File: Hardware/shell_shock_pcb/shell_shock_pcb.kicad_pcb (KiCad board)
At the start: 2 copper layers, 30 parts, among them U14 LT3080EDD-PBF, U23 LT3080EDD-PBF, U4 LT3080EDD-PBF, U5 LT3080EDD-PBF

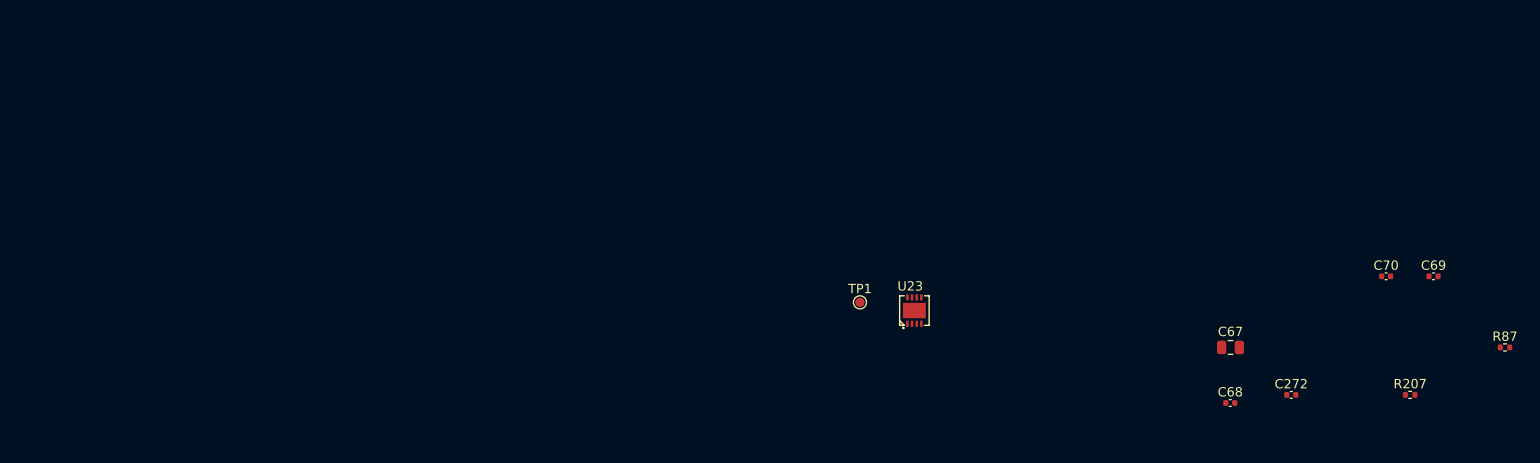
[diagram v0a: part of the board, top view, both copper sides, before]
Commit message: Added hardware tools
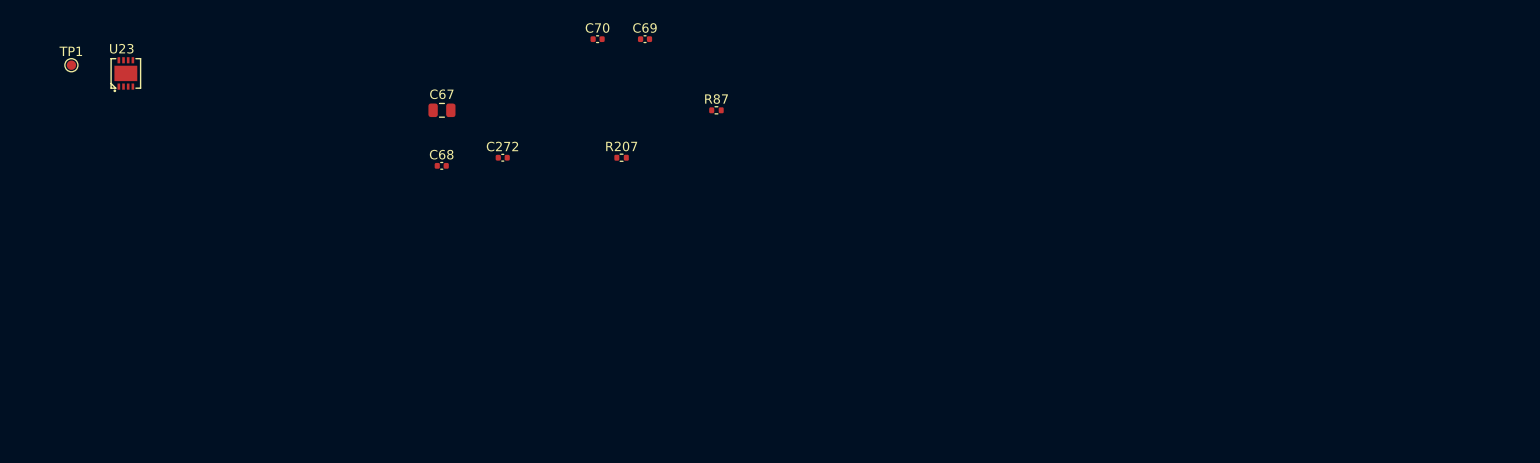
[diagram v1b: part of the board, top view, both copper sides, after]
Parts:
- moved C68 88.2 mm to (145.7, 82.1)
- moved C69 88.2 mm to (167.5, 68.6)
- moved C70 88.2 mm to (162.4, 68.6)
- moved R207 88.2 mm to (165.0, 81.3)
- moved U23 88.2 mm to (111.9, 72.2)
- moved C67 88.2 mm to (145.7, 76.2)
- moved C272 88.2 mm to (152.2, 81.3)
- moved TP1 88.2 mm to (106.0, 71.4)
- moved R87 88.2 mm to (175.1, 76.2)
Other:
- board text added: "1.5V - PS"
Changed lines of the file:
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@@
   (net 13 "unconnected-(U23-NC-Pad6)")
   (footprint "Capacitor_SMD:C_0402_1005Metric" (layer "F.Cu")
-    (at 236.7 106.68)
+    (at 152.24 81.28)
     (descr "Capacitor SMD 0402 (1005 Metric), square (rectangular) end terminal, IPC_7351 nominal, (Body size source: IPC-SM-782 page 76, https://www.pcb-3d.com/wordpress/wp-content/uploads/ipc-sm-782a_amendment_1_and_2.pdf), generated with kicad-footprint-generator")
     (tags "capacitor")
@@
   )
   (footprint "Capacitor_SMD:C_0402_1005Metric" (layer "F.Cu")
-    (at 251.94 93.98)
+    (at 167.48 68.58)
     (descr "Capacitor SMD 0402 (1005 Metric), square (rectangular) end terminal, IPC_7351 nominal, (Body size source: IPC-SM-782 page 76, https://www.pcb-3d.com/wordpress/wp-content/uploads/ipc-sm-782a_amendment_1_and_2.pdf), generated with kicad-footprint-generator")
     (tags "capacitor")
@@
   )
   (footprint "Capacitor_SMD:C_0402_1005Metric" (layer "F.Cu")
-    (at 230.166096 107.549422)
+    (at 145.706096 82.149422)
     (descr "Capacitor SMD 0402 (1005 Metric), square (rectangular) end terminal, IPC_7351 nominal, (Body size source: IPC-SM-782 page 76, https://www.pcb-3d.com/wordpress/wp-content/uploads/ipc-sm-782a_amendment_1_and_2.pdf), generated with kicad-footprint-generator")
     (tags "capacitor")
@@
   )
   (footprint "Capacitor_SMD:C_0402_1005Metric" (layer "F.Cu")
-    (at 246.86 93.98)
+    (at 162.4 68.58)
     (descr "Capacitor SMD 0402 (1005 Metric), square (rectangular) end terminal, IPC_7351 nominal, (Body size source: IPC-SM-782 page 76, https://www.pcb-3d.com/wordpress/wp-content/uploads/ipc-sm-782a_amendment_1_and_2.pdf), generated with kicad-footprint-generator")
     (tags "capacitor")
@@
   )
   (footprint "Resistor_SMD:R_0402_1005Metric" (layer "F.Cu")
-    (at 249.43 106.68)
+    (at 164.97 81.28)
     (descr "Resistor SMD 0402 (1005 Metric), square (rectangular) end terminal, IPC_7351 nominal, (Body size source: IPC-SM-782 page 72, https://www.pcb-3d.com/wordpress/wp-content/uploads/ipc-sm-782a_amendment_1_and_2.pdf), generated with kicad-footprint-generator")
     (tags "resistor")
@@
   )
   (footprint "Resistor_SMD:R_0402_1005Metric" (layer "F.Cu")
-    (at 259.59 101.6)
+    (at 175.13 76.2)
     (descr "Resistor SMD 0402 (1005 Metric), square (rectangular) end terminal, IPC_7351 nominal, (Body size source: IPC-SM-782 page 72, https://www.pcb-3d.com/wordpress/wp-content/uploads/ipc-sm-782a_amendment_1_and_2.pdf), generated with kicad-footprint-generator")
     (tags "resistor")
@@
   )
   (footprint "TestPoint:TestPoint_Pad_D1.0mm" (layer "F.Cu")
-    (at 190.5 96.77)
+    (at 106.04 71.37)
     (descr "SMD pad as test Point, diameter 1.0mm")
     (tags "test point SMD pad")
@@
   )
   (footprint "Capacitor_SMD:C_0805_2012Metric" (layer "F.Cu")
-    (at 230.19 101.6)
+    (at 145.73 76.2)
     (descr "Capacitor SMD 0805 (2012 Metric), square (rectangular) end terminal, IPC_7351 nominal, (Body size source: IPC-SM-782 page 76, https://www.pcb-3d.com/wordpress/wp-content/uploads/ipc-sm-782a_amendment_1_and_2.pdf, https://docs.google.com/spreadsheets/d/1BsfQQcO9C6DZCsRaXUlFlo91Tg2WpOkGARC1WS5S8t0/edit?usp=sharing), generated with kicad-footprint-generator")
     (tags "capacitor")
@@
   )
   (footprint "LCSC:DFN-8_L3.0-W3.0-P0.50-BL-EP" (layer "F.Cu")
-    (at 196.33 97.65)
+    (at 111.87 72.25)
     (property "LCSC" "C462675")
     (property "Sheetfile" "shell_shock_pcb.kicad_sch")
@@
     (effects (font (size 1 1) (thickness 0.15)) (justify left bottom))
   )
-  (gr_text "1.8V - PS" (at 43.425782 194.156525) (layer "Dwgs.User")
+  (gr_text "1.5V - PS" (at 43.425782 194.156525) (layer "Dwgs.User")
     (effects (font (size 1 1) (thickness 0.15)) (justify left bottom))
   )

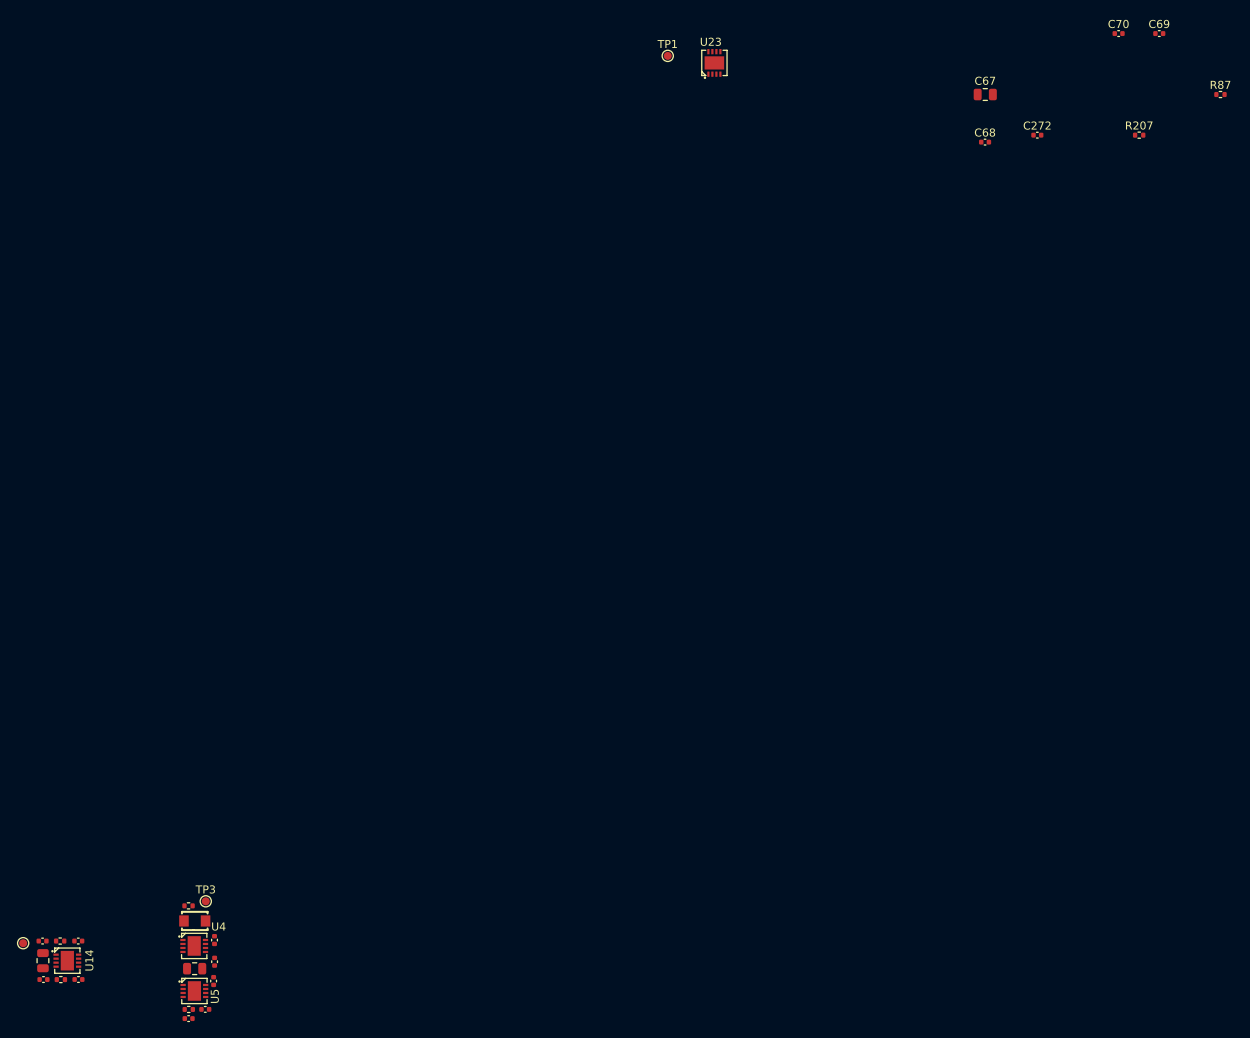
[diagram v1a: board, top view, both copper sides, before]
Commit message: sketch pcb for LT3080 ps
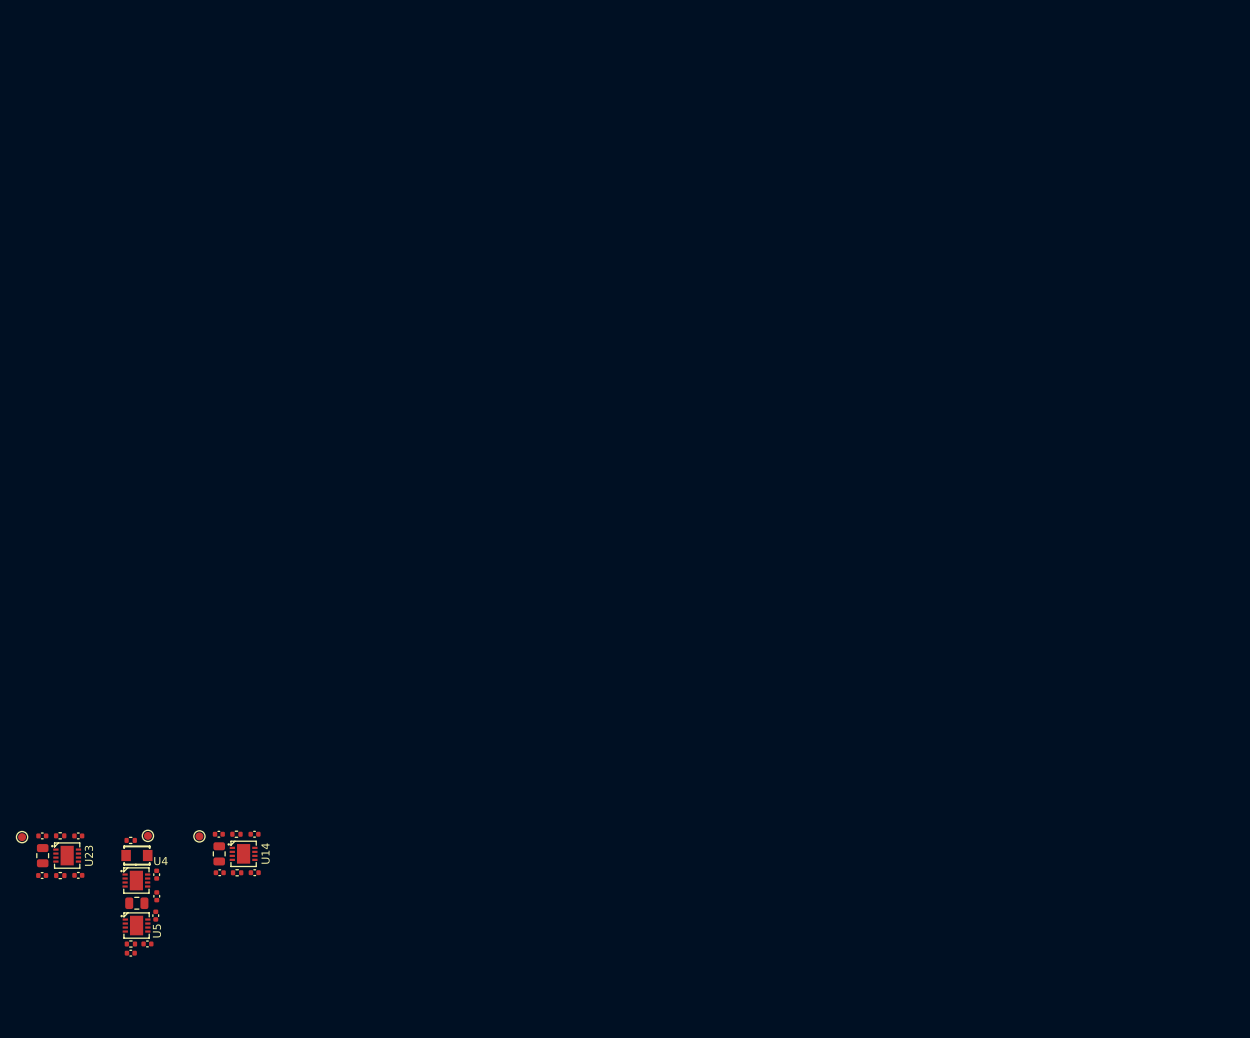
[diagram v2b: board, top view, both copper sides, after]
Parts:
- moved R87 172.1 mm to (30.1, 168.9)
- moved C69 171.3 mm to (32.4, 173.8), turned to 180 degrees
- moved C70 164.2 mm to (32.4, 168.9), turned to 180 degrees
- moved R207 163.6 mm to (30.1, 173.8)
- moved C272 155.0 mm to (27.8, 173.8), turned to 180 degrees
- moved C67 151.4 mm to (27.9, 171.3), turned to -90 degrees
- moved C68 146.3 mm to (27.9, 168.9)
- moved U23 127.9 mm to (31.0, 171.3), turned to -90 degrees
- moved TP1 126.7 mm to (25.3, 169.0)
- moved R2 25.8 mm to (52.1, 168.7)
- moved C54 25.8 mm to (49.9, 168.7)
- moved C234 25.8 mm to (50.0, 173.5)
- moved C48 25.8 mm to (54.4, 168.7)
- moved C53 25.8 mm to (50.0, 171.1)
- moved R172 25.8 mm to (52.2, 173.5)
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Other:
- board text added: "1.2V - PS"
